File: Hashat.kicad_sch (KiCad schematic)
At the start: 7 parts

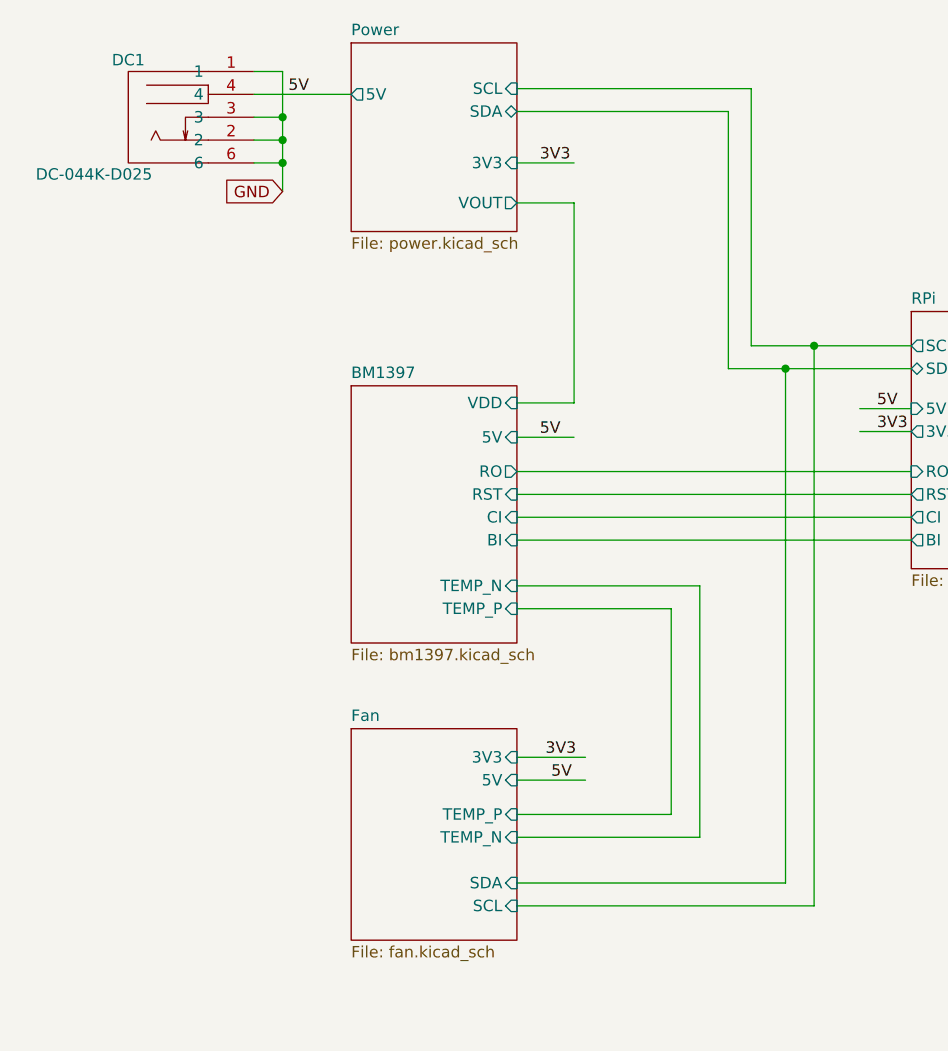
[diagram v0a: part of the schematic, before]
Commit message: cleanup. added LCSC fan connector
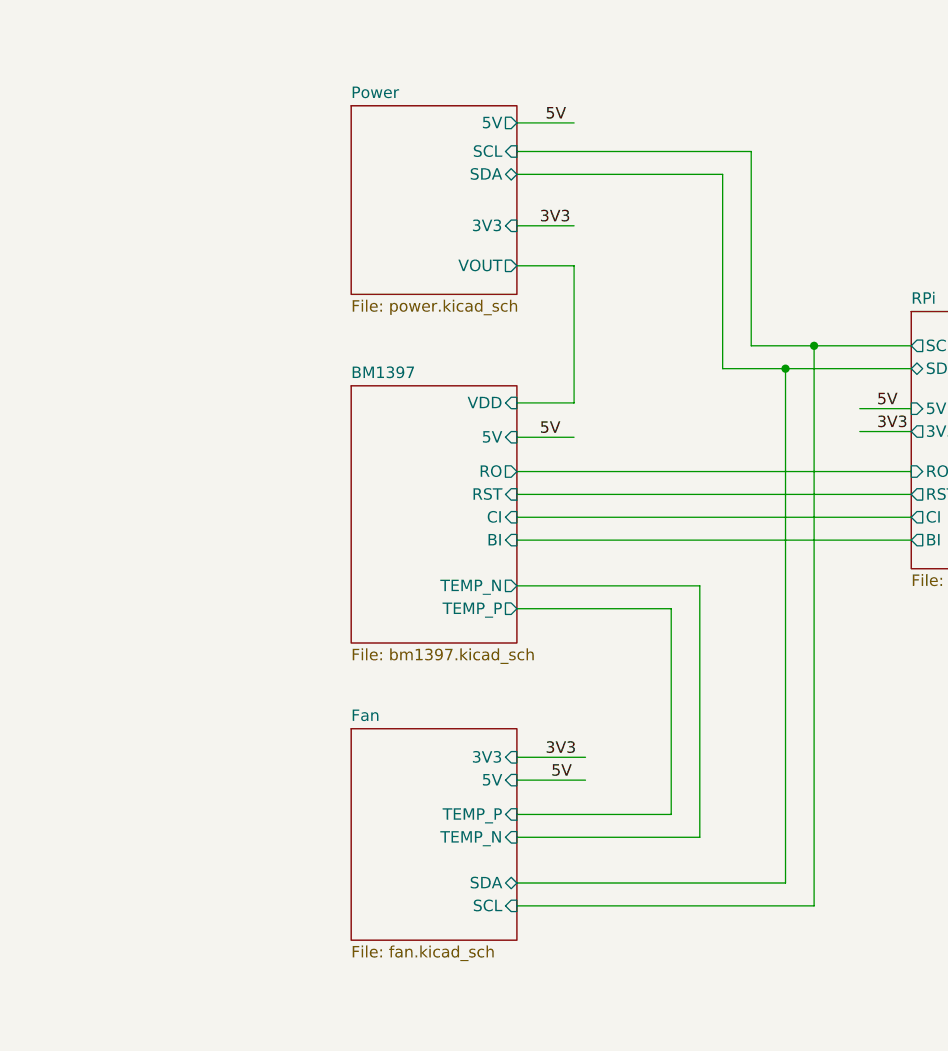
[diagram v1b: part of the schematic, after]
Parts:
- removed DC1: DC-044K-D025, lcsc:DC-IN-TH_DC-044K-D025, symbol lcsc:DC-044K-D025
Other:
- title: (none) -> The Hashat
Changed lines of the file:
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@@
   (paper "A4")
   (title_block
+    (title "The Hashat")
     (date "2023-04-21")
-  )
-  (junction (at 71.755 48.26) (diameter 0) (color 0 0 0 0)
+    (rev "1")
   )
   (junction (at 130.81 73.66) (diameter 0) (color 0 0 0 0)
   )
-  (junction (at 71.755 50.8) (diameter 0) (color 0 0 0 0)
-  )
   (junction (at 127.635 76.2) (diameter 0) (color 0 0 0 0)
   )
-  (junction (at 71.755 53.34) (diameter 0) (color 0 0 0 0)
-  )
-  (wire (pts (xy 97.79 53.34) (xy 104.14 53.34))
-    (stroke (width 0) (type default))
-  )
-  (wire (pts (xy 71.755 48.26) (xy 71.755 50.8))
-    (stroke (width 0) (type default))
-  )
-  (wire (pts (xy 121.285 76.2) (xy 127.635 76.2))
-    (stroke (width 0) (type default))
-  )
-  (wire (pts (xy 97.79 57.785) (xy 104.14 57.785))
-    (stroke (width 0) (type default))
-  )
-  (wire (pts (xy 123.825 45.085) (xy 97.79 45.085))
-    (stroke (width 0) (type default))
-  )
-  (wire (pts (xy 97.79 47.625) (xy 121.285 47.625))
+  (wire (pts (xy 97.79 60.325) (xy 104.14 60.325))
+    (stroke (width 0) (type default))
+  )
+  (wire (pts (xy 120.65 76.2) (xy 127.635 76.2))
+    (stroke (width 0) (type default))
+  )
+  (wire (pts (xy 97.79 64.77) (xy 104.14 64.77))
+    (stroke (width 0) (type default))
+  )
+  (wire (pts (xy 123.825 52.07) (xy 97.79 52.07))
+    (stroke (width 0) (type default))
+  )
+  (wire (pts (xy 97.79 54.61) (xy 120.65 54.61))
     (stroke (width 0) (type default))
   )
@@
     (stroke (width 0) (type default))
   )
-  (wire (pts (xy 121.285 47.625) (xy 121.285 76.2))
-    (stroke (width 0) (type default))
-  )
-  (wire (pts (xy 68.58 48.26) (xy 71.755 48.26))
+  (wire (pts (xy 120.65 54.61) (xy 120.65 76.2))
     (stroke (width 0) (type default))
   )
@@
     (stroke (width 0) (type default))
   )
-  (wire (pts (xy 68.58 43.18) (xy 71.755 43.18))
-    (stroke (width 0) (type default))
-  )
   (wire (pts (xy 97.79 83.82) (xy 104.14 83.82))
     (stroke (width 0) (type default))
@@
     (stroke (width 0) (type default))
   )
-  (wire (pts (xy 68.58 50.8) (xy 71.755 50.8))
-    (stroke (width 0) (type default))
-  )
   (wire (pts (xy 97.79 135.89) (xy 130.81 135.89))
     (stroke (width 0) (type default))
@@
     (stroke (width 0) (type default))
   )
-  (wire (pts (xy 68.58 53.34) (xy 71.755 53.34))
-    (stroke (width 0) (type default))
-  )
   (wire (pts (xy 97.79 90.17) (xy 141.605 90.17))
     (stroke (width 0) (type default))
   )
-  (wire (pts (xy 68.58 45.72) (xy 79.375 45.72))
-    (stroke (width 0) (type default))
-  )
   (wire (pts (xy 141.605 73.66) (xy 130.81 73.66))
     (stroke (width 0) (type default))
   )
-  (wire (pts (xy 71.755 53.34) (xy 71.755 56.515))
-    (stroke (width 0) (type default))
-  )
-  (wire (pts (xy 71.755 50.8) (xy 71.755 53.34))
-    (stroke (width 0) (type default))
-  )
   (wire (pts (xy 97.79 100.33) (xy 118.11 100.33))
     (stroke (width 0) (type default))
@@
     (stroke (width 0) (type default))
   )
-  (wire (pts (xy 123.825 73.66) (xy 123.825 45.085))
+  (wire (pts (xy 123.825 73.66) (xy 123.825 52.07))
     (stroke (width 0) (type default))
   )
@@
     (stroke (width 0) (type default))
   )
+  (wire (pts (xy 97.79 48.895) (xy 104.14 48.895))
+    (stroke (width 0) (type default))
+  )
   (wire (pts (xy 130.81 135.89) (xy 130.81 73.66))
     (stroke (width 0) (type default))
   )
-  (wire (pts (xy 104.14 57.785) (xy 104.14 80.01))
+  (wire (pts (xy 104.14 64.77) (xy 104.14 80.01))
     (stroke (width 0) (type default))
   )
@@
     (stroke (width 0) (type default))
   )
-  (wire (pts (xy 71.755 43.18) (xy 71.755 48.26))
-    (stroke (width 0) (type default))
-  )
   (wire (pts (xy 97.79 119.38) (xy 105.41 119.38))
     (stroke (width 0) (type default))
@@
     (effects (font (size 1.27 1.27)) (justify left bottom))
   )
-  (label "3V3" (at 100.33 53.34 0) (fields_autoplaced)
+  (label "3V3" (at 100.33 60.325 0) (fields_autoplaced)
     (effects (font (size 1.27 1.27)) (justify left bottom))
   )
@@
     (effects (font (size 1.27 1.27)) (justify left bottom))
   )
-  (label "5V" (at 72.39 45.72 0) (fields_autoplaced)
+  (label "5V" (at 100.965 48.895 0) (fields_autoplaced)
     (effects (font (size 1.27 1.27)) (justify left bottom))
   )
@@
     (effects (font (size 1.27 1.27)) (justify left bottom))
   )
-  (global_label "GND" (shape input) (at 71.755 56.515 180) (fields_autoplaced)
-    (effects (font (size 1.27 1.27)) (justify right))
-    (property "Intersheetrefs" "${INTERSHEET_REFS}" (at 65.6329 56.515 0)
-      (effects (font (size 1.27 1.27)) (justify right) hide)
-    )
-  )
   (symbol (lib_id "Mechanical:MountingHole") (at 74.93 173.355 0) (unit 1)
     (in_bom yes) (on_board yes) (dnp no) (fields_autoplaced)
@@
         (path "/e63e39d7-6ac0-4ffd-8aa3-1841a4541b55"
           (reference "H5") (unit 1)
-        )
-      )
-    )
-  )
-  (symbol (lib_id "lcsc:DC-044K-D025") (at 60.96 48.26 0) (unit 1)
-    (in_bom yes) (on_board yes) (dnp no)
-    (property "Reference" "DC1" (at 54.61 41.91 0)
-      (effects (font (size 1.27 1.27)))
-    )
-    (property "Value" "DC-044K-D025" (at 50.8 54.61 0)
-      (effects (font (size 1.27 1.27)))
-    )
-    (property "Footprint" "lcsc:DC-IN-TH_DC-044K-D025" (at 60.96 60.96 0)
-      (effects (font (size 1.27 1.27)) hide)
-    )
-    (property "Datasheet" "" (at 60.96 48.26 0)
-      (effects (font (size 1.27 1.27)) hide)
-    )
-    (property "Manufacturer" "G-Switch" (at 60.96 63.5 0)
-      (effects (font (size 1.27 1.27)) hide)
-    )
-    (property "LCSC Part" "C963204" (at 60.96 66.04 0)
-      (effects (font (size 1.27 1.27)) hide)
-    )
-    (property "JLC Part" "Extended Part" (at 60.96 68.58 0)
-      (effects (font (size 1.27 1.27)) hide)
-    )
-    (pin "1")
-    (pin "2")
-    (pin "3")
-    (pin "4")
-    (pin "6")
-    (instances
-      (project "Hashat"
-        (path "/00740941-7ad8-466a-a267-188591e2b5c4"
-          (reference "DC1") (unit 1)
         )
       )
@@
       (effects (font (size 1.27 1.27)) (justify right))
     )
-    (pin "TEMP_N" input (at 97.79 100.33 0)
-      (effects (font (size 1.27 1.27)) (justify right))
-    )
-    (pin "TEMP_P" input (at 97.79 102.87 0)
+    (pin "TEMP_N" output (at 97.79 100.33 0)
+      (effects (font (size 1.27 1.27)) (justify right))
+    )
+    (pin "TEMP_P" output (at 97.79 102.87 0)
       (effects (font (size 1.27 1.27)) (justify right))
     )
@@
     )
   )
-  (sheet (at 79.375 40.005) (size 18.415 20.955) (fields_autoplaced)
+  (sheet (at 79.375 46.99) (size 18.415 20.955) (fields_autoplaced)
     (stroke (width 0.1524) (type solid))
     (fill (color 255 255 194 1.0000))
-    (property "Sheetname" "Power" (at 79.375 39.2934 0)
+    (property "Sheetname" "Power" (at 79.375 46.2784 0)
       (effects (font (size 1.27 1.27)) (justify left bottom))
     )
-    (property "Sheetfile" "power.kicad_sch" (at 79.375 61.5446 0)
+    (property "Sheetfile" "power.kicad_sch" (at 79.375 68.5296 0)
       (effects (font (size 1.27 1.27)) (justify left top))
     )
-    (pin "VOUT" output (at 97.79 57.785 0)
-      (effects (font (size 1.27 1.27)) (justify right))
-    )
-    (pin "SCL" input (at 97.79 45.085 0)
-      (effects (font (size 1.27 1.27)) (justify right))
-    )
-    (pin "SDA" bidirectional (at 97.79 47.625 0)
-      (effects (font (size 1.27 1.27)) (justify right))
-    )
-    (pin "3V3" input (at 97.79 53.34 0)
-      (effects (font (size 1.27 1.27)) (justify right))
-    )
-    (pin "5V" output (at 79.375 45.72 180)
-      (effects (font (size 1.27 1.27)) (justify left))
+    (pin "VOUT" output (at 97.79 64.77 0)
+      (effects (font (size 1.27 1.27)) (justify right))
+    )
+    (pin "SCL" input (at 97.79 52.07 0)
+      (effects (font (size 1.27 1.27)) (justify right))
+    )
+    (pin "SDA" bidirectional (at 97.79 54.61 0)
+      (effects (font (size 1.27 1.27)) (justify right))
+    )
+    (pin "3V3" input (at 97.79 60.325 0)
+      (effects (font (size 1.27 1.27)) (justify right))
+    )
+    (pin "5V" output (at 97.79 48.895 0)
+      (effects (font (size 1.27 1.27)) (justify right))
     )
     (instances
@@
       (effects (font (size 1.27 1.27)) (justify right))
     )
-    (pin "SDA" input (at 97.79 133.35 0)
-      (effects (font (size 1.27 1.27)) (justify right))
-    )
+    (pin "SDA" bidirectional (at 97.79 133.35 0)
+      (effects (font (size 1.27 1.27)) (justify right))
+    )

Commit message: added webench design docs
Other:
- note added: "to the moon!"
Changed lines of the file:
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@@
     (stroke (width 0) (type default))
+  )
+  (text "to the moon!" (at 182.245 177.165 0)
+    (effects (font (size 5 5) (thickness 1) bold italic) (justify left bottom))
   )
   (label "5V" (at 137.795 80.645 0) (fields_autoplaced)

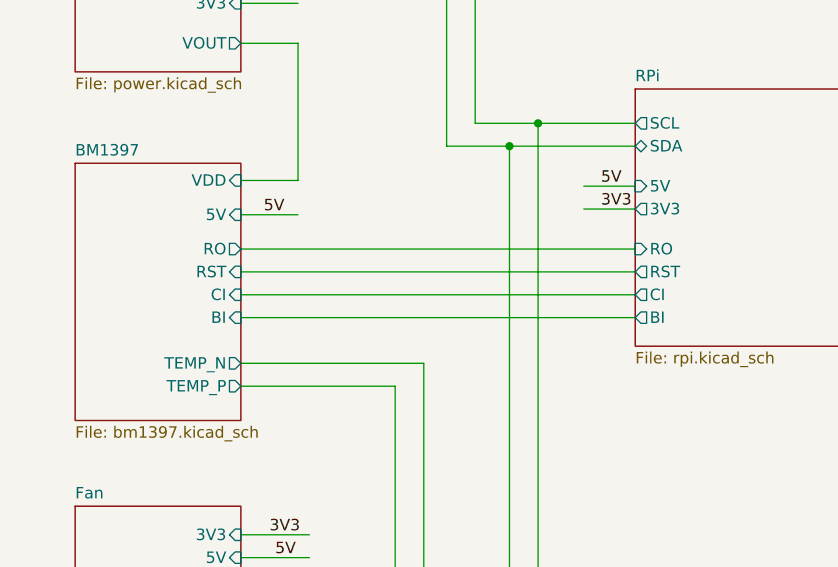
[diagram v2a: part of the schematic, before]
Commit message: cleanup level shifters. LCRC inductor for buck
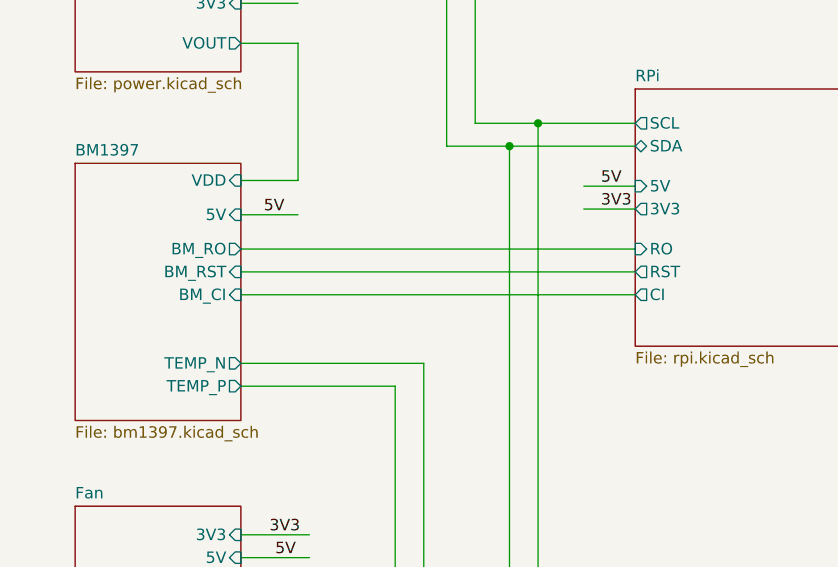
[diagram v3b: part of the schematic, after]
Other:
- sheet BM1397 ports: added BM_CI, BM_RO, BM_RST; removed BI, CI, RO, RST
- sheet RPi ports: added none; removed BI
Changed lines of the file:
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@@
-    (stroke (width 0) (type default))
-  )
-  (wire (pts (xy 97.79 95.25) (xy 141.605 95.25))
     (stroke (width 0) (type default))
   )
@@
       (effects (font (size 1.27 1.27)) (justify left))
     )
-    (pin "BI" output (at 141.605 95.25 180)
-      (effects (font (size 1.27 1.27)) (justify left))
-    )
     (pin "RST" output (at 141.605 90.17 180)
       (effects (font (size 1.27 1.27)) (justify left))
@@
       (effects (font (size 1.27 1.27)) (justify right))
     )
-    (pin "RO" output (at 97.79 87.63 0)
-      (effects (font (size 1.27 1.27)) (justify right))
-    )
-    (pin "RST" input (at 97.79 90.17 0)
-      (effects (font (size 1.27 1.27)) (justify right))
-    )
-    (pin "CI" input (at 97.79 92.71 0)
-      (effects (font (size 1.27 1.27)) (justify right))
-    )
-    (pin "BI" input (at 97.79 95.25 0)
-      (effects (font (size 1.27 1.27)) (justify right))
-    )
+    (pin "BM_RO" output (at 97.79 87.63 0)
+      (effects (font (size 1.27 1.27)) (justify right))
+    )
+    (pin "BM_CI" input (at 97.79 92.71 0)
+      (effects (font (size 1.27 1.27)) (justify right))
+    )
+    (pin "BM_RST" input (at 97.79 90.17 0)
+      (effects (font (size 1.27 1.27)) (justify right))
+    )

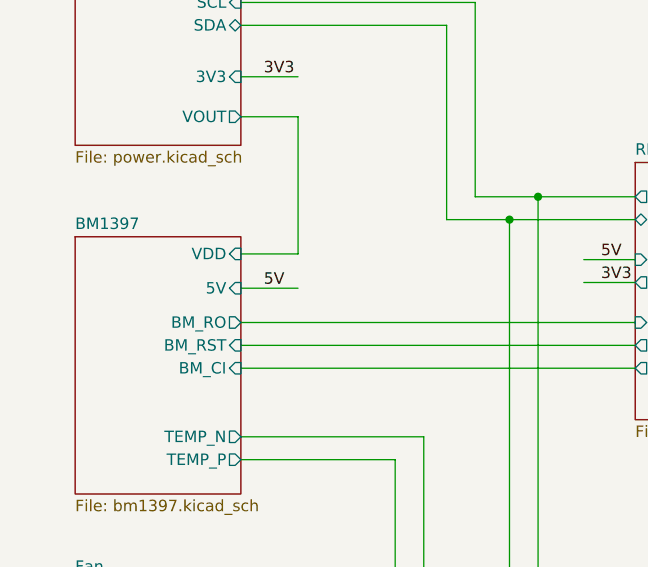
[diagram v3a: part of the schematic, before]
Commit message: pretty much all the signals are routed
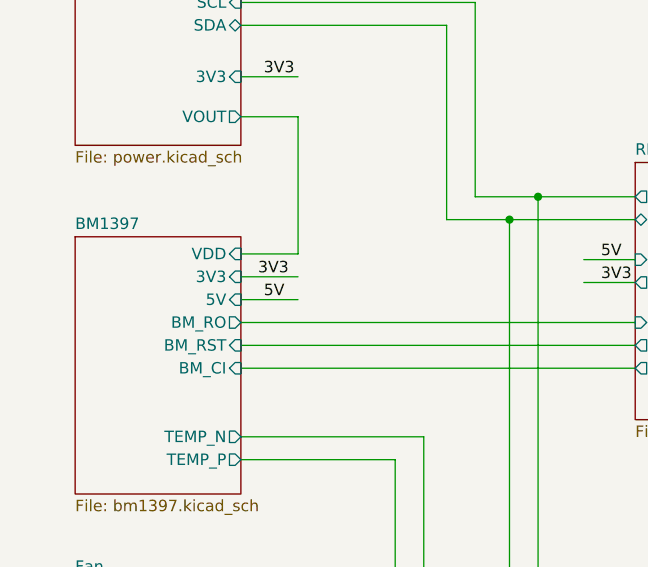
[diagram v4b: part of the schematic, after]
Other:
- sheet BM1397 ports: added 3V3; removed none
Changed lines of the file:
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@@
-    (stroke (width 0) (type default))
-  )
-  (wire (pts (xy 97.79 83.82) (xy 104.14 83.82))
     (stroke (width 0) (type default))
   )
@@
     (stroke (width 0) (type default))
   )
+  (wire (pts (xy 97.79 85.09) (xy 104.14 85.09))
+    (stroke (width 0) (type default))
+  )
   (wire (pts (xy 118.11 100.33) (xy 118.11 128.27))
     (stroke (width 0) (type default))
@@
   )
   (wire (pts (xy 104.14 80.01) (xy 97.79 80.01))
+    (stroke (width 0) (type default))
+  )
+  (wire (pts (xy 97.79 82.55) (xy 104.14 82.55))
     (stroke (width 0) (type default))
   )
@@
     (effects (font (size 1.27 1.27)) (justify left bottom))
   )
-  (label "5V" (at 100.33 83.82 0) (fields_autoplaced)
+  (label "3V3" (at 99.695 82.55 0) (fields_autoplaced)
+    (effects (font (size 1.27 1.27)) (justify left bottom))
+  )
+  (label "5V" (at 100.33 85.09 0) (fields_autoplaced)
     (effects (font (size 1.27 1.27)) (justify left bottom))
   )
@@
       (effects (font (size 1.27 1.27)) (justify right))
     )
-    (pin "5V" input (at 97.79 83.82 0)
+    (pin "5V" input (at 97.79 85.09 0)
       (effects (font (size 1.27 1.27)) (justify right))
     )
@@
       (effects (font (size 1.27 1.27)) (justify right))
     )
+    (pin "3V3" input (at 97.79 82.55 0)
+      (effects (font (size 1.27 1.27)) (justify right))
+    )
